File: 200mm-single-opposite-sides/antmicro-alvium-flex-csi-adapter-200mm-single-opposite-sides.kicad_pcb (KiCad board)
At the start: 2 copper layers, 25.5 x 200.1 mm, 3 parts, among them J1 WE_687622100002_FLEX, J2 WE_687650100002_FLEX

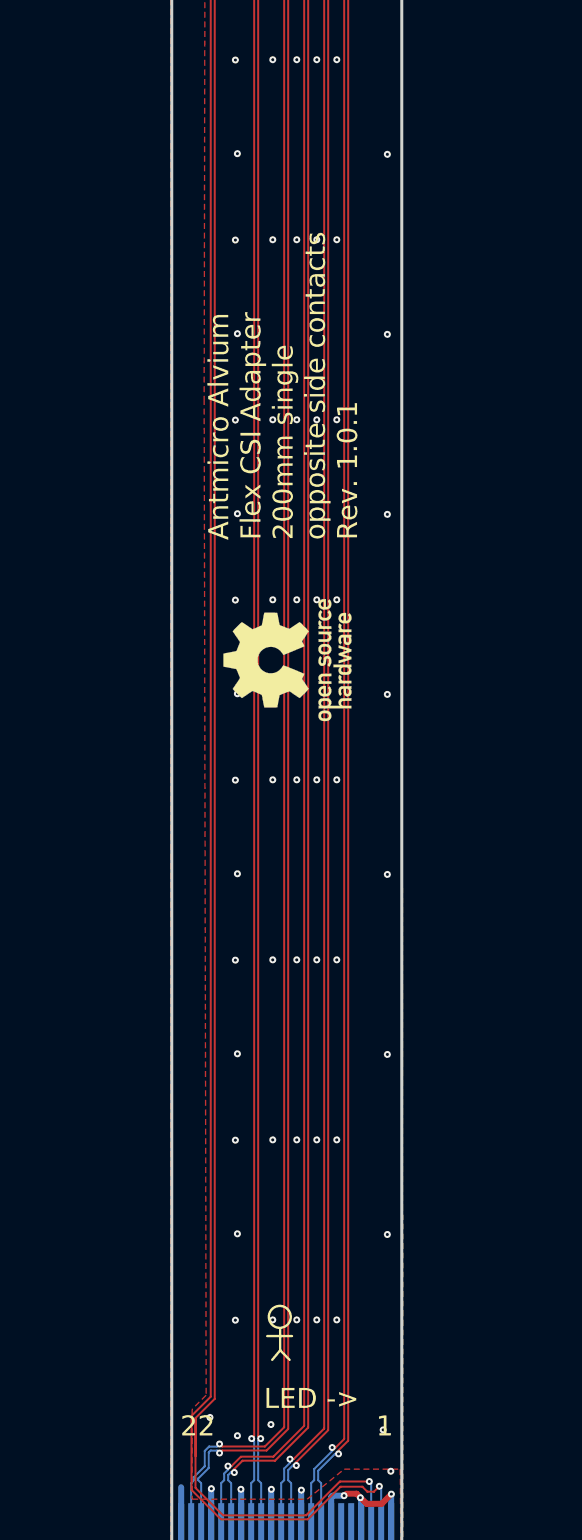
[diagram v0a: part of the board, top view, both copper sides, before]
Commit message: Update naming convention for the 200mm single
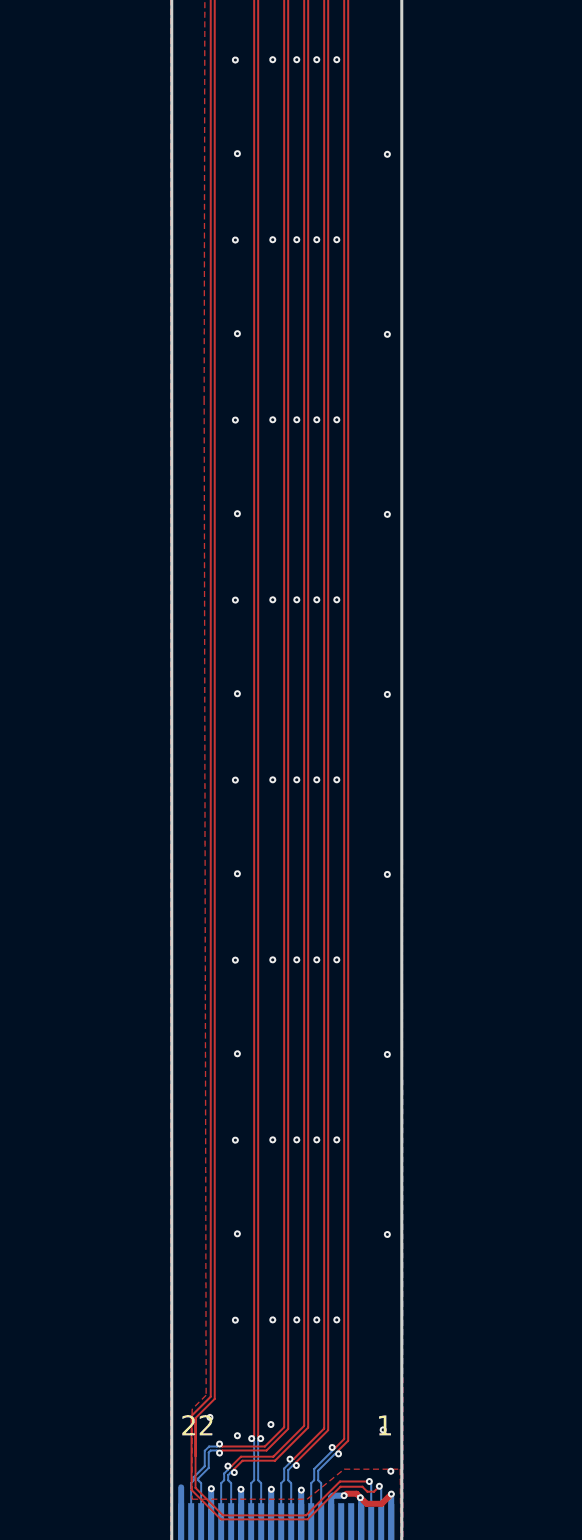
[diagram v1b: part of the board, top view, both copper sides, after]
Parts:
- N1: moved to B.Cu
- moved N1 10.4 mm to (189.0, 208.2), turned to 270 degrees
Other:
- board text added: "<- LED"
- board text removed: "LED ->"

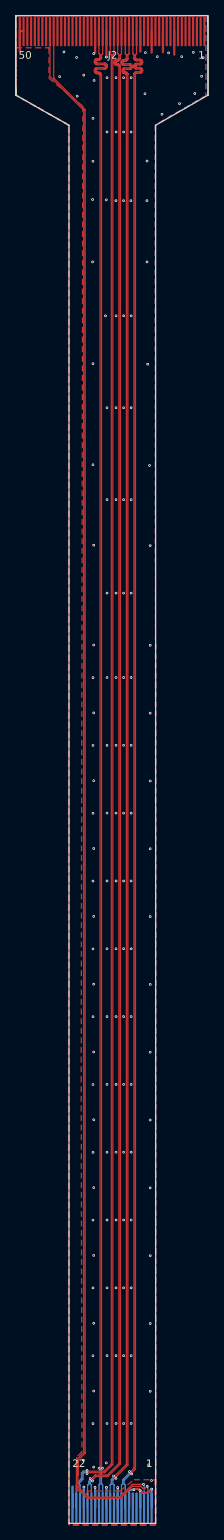
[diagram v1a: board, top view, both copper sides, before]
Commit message: 200mm-single-opposite: add NMOS transistor for camera triggering
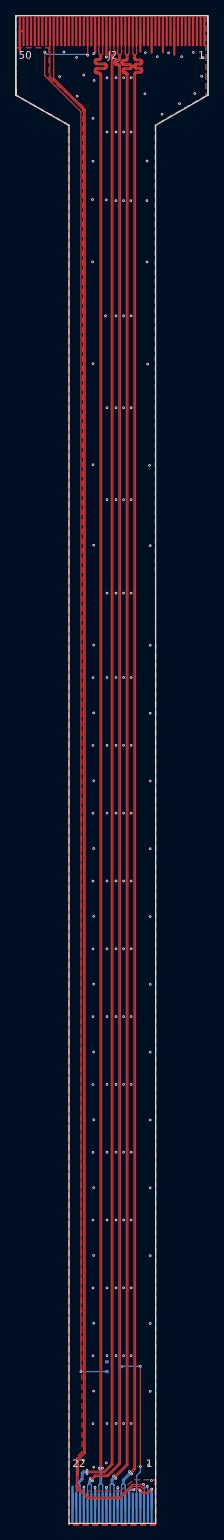
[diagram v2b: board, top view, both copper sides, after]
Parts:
- added Q1: BSS138APW, antmicro-alvium-flex-csi-adapter-footprints:SC70-3, B.Cu at (189.0, 244.0)
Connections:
- J2 pad 32: Net-(J2-Pad32) -> /VSYNC
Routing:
- net /VSYNC: track 0.00 -> 189.7 mm, vias 0 -> 3
- net /GPIO2: track 0.00 -> 21.5 mm, vias 0 -> 2
